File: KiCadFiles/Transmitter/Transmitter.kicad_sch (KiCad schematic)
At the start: 5 parts, among them J1 AM-Joystick, SW1 SW_Push, SW2 SW_Push, U1 NRF24L01_Breakout

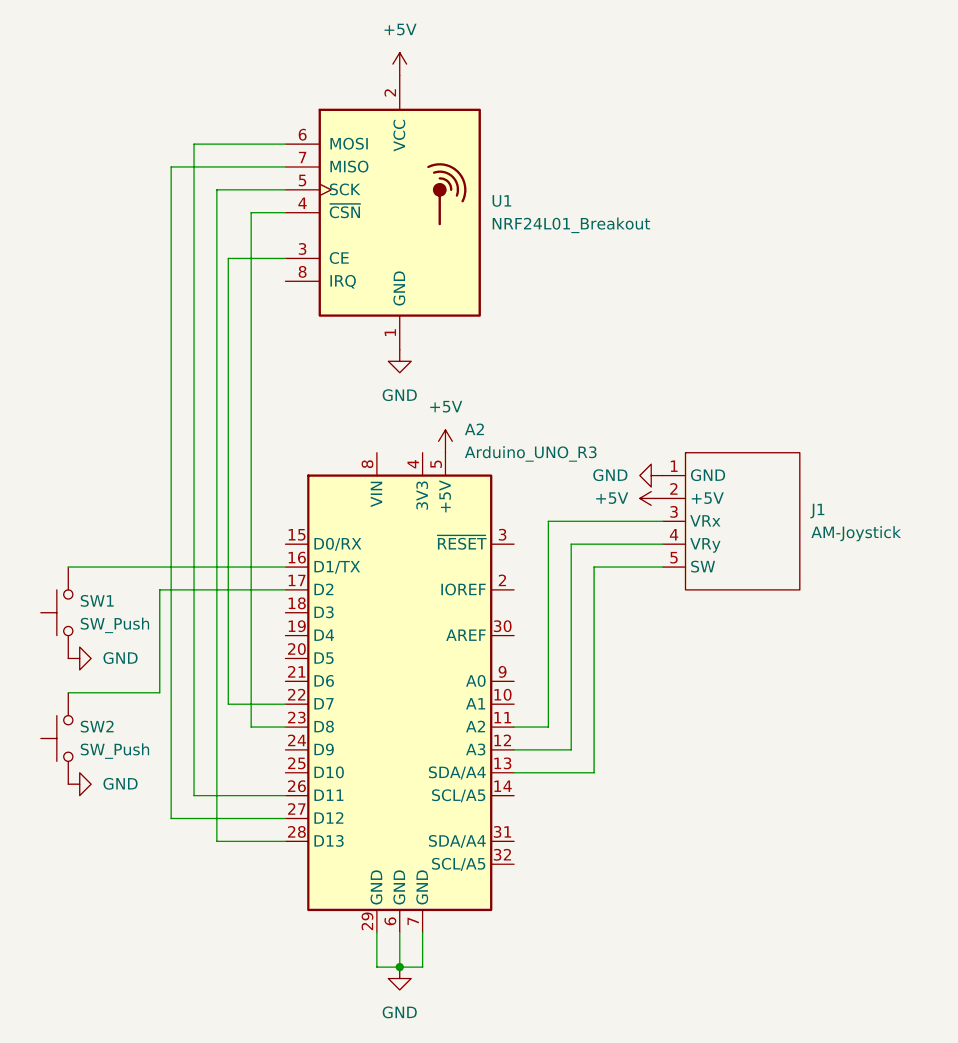
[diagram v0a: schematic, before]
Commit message: Add more buttons, modify schematic, and change code (#6)
* Add more buttons, update schematic, improve drive system

* Change button pins, schematic, and add quarter speed
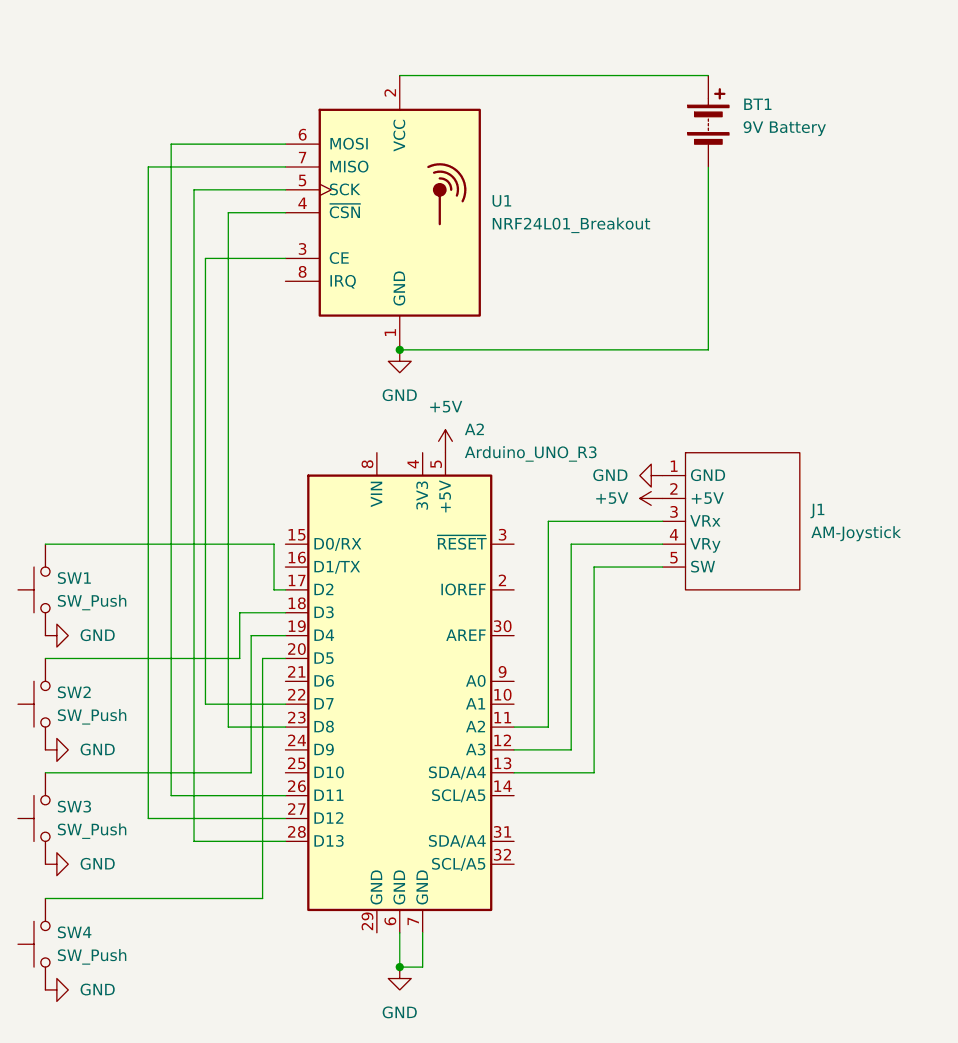
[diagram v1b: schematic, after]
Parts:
- added BT1: 9V Battery, symbol Device:Battery
- added SW3, SW4: SW_Push, symbol Switch:SW_Push
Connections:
- net +5V: no longer U1.2 (VCC)
- net GND: now also BT1.2 (-), SW3.1, SW4.1; no longer A2.29 (GND)
- net at A2.16 (D1/TX): no longer SW1.2
- net at A2.17 (D2): now also SW1.2; no longer SW2.2
- net at A2.18 (D3): now also SW2.2
- net at A2.19 (D4): now also SW3.2
- net at A2.20 (D5): now also SW4.2
- new net: BT1.1 (+), U1.2 (VCC)
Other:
- moved on the sheet: SW1, SW2
